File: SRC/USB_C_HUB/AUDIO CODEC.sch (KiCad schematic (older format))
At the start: 16 parts, among them IC6 ADAU1961WBCPZ-R7, J9 AudioJack2_Ground

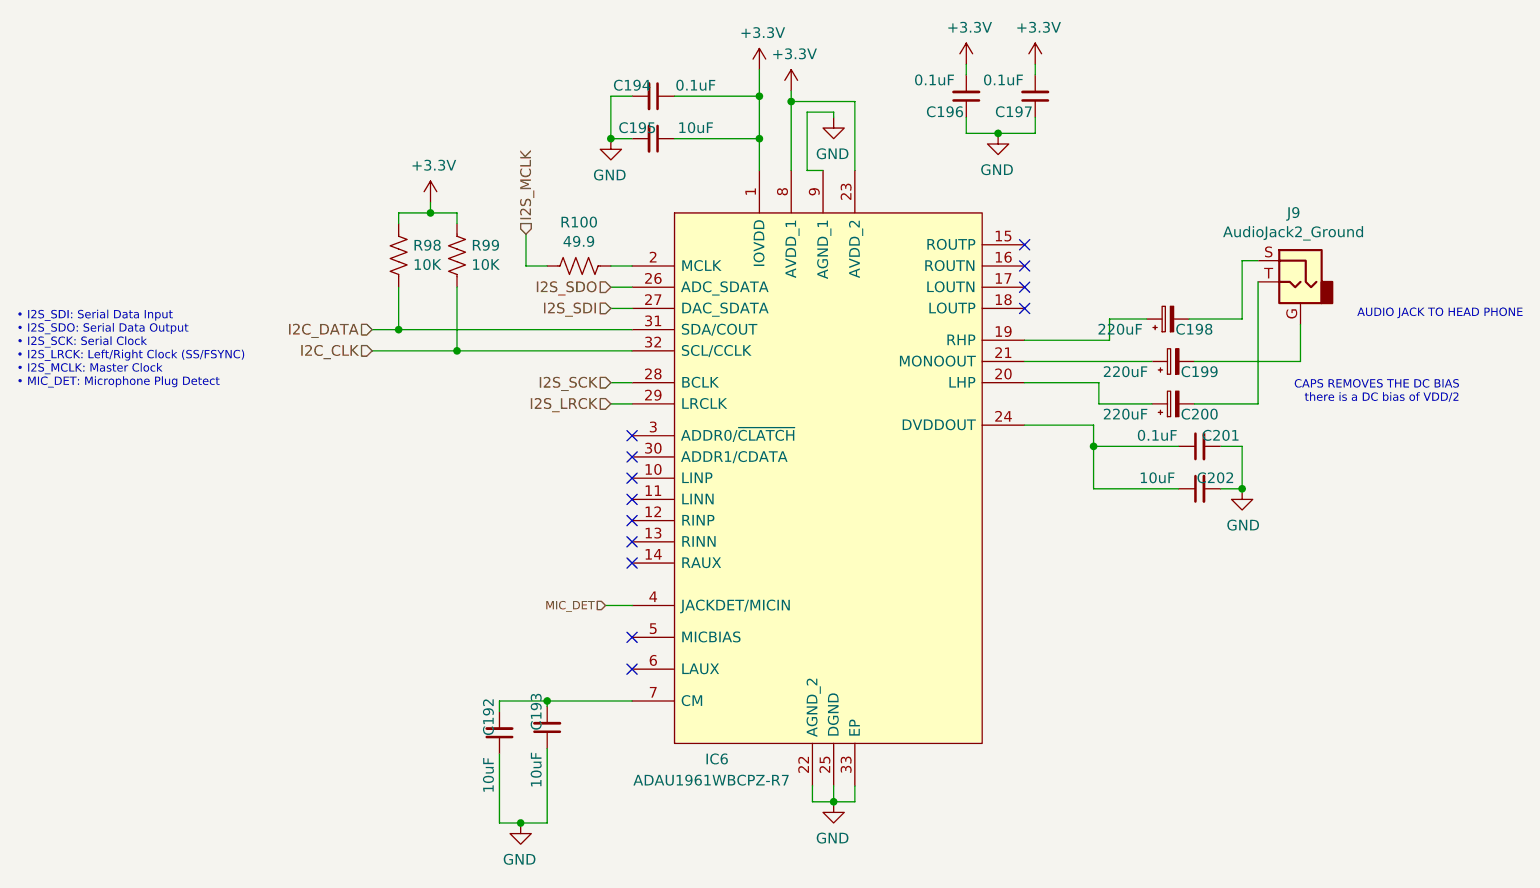
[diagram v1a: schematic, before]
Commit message: schematic capture and footprint assignment complete. Pending approval
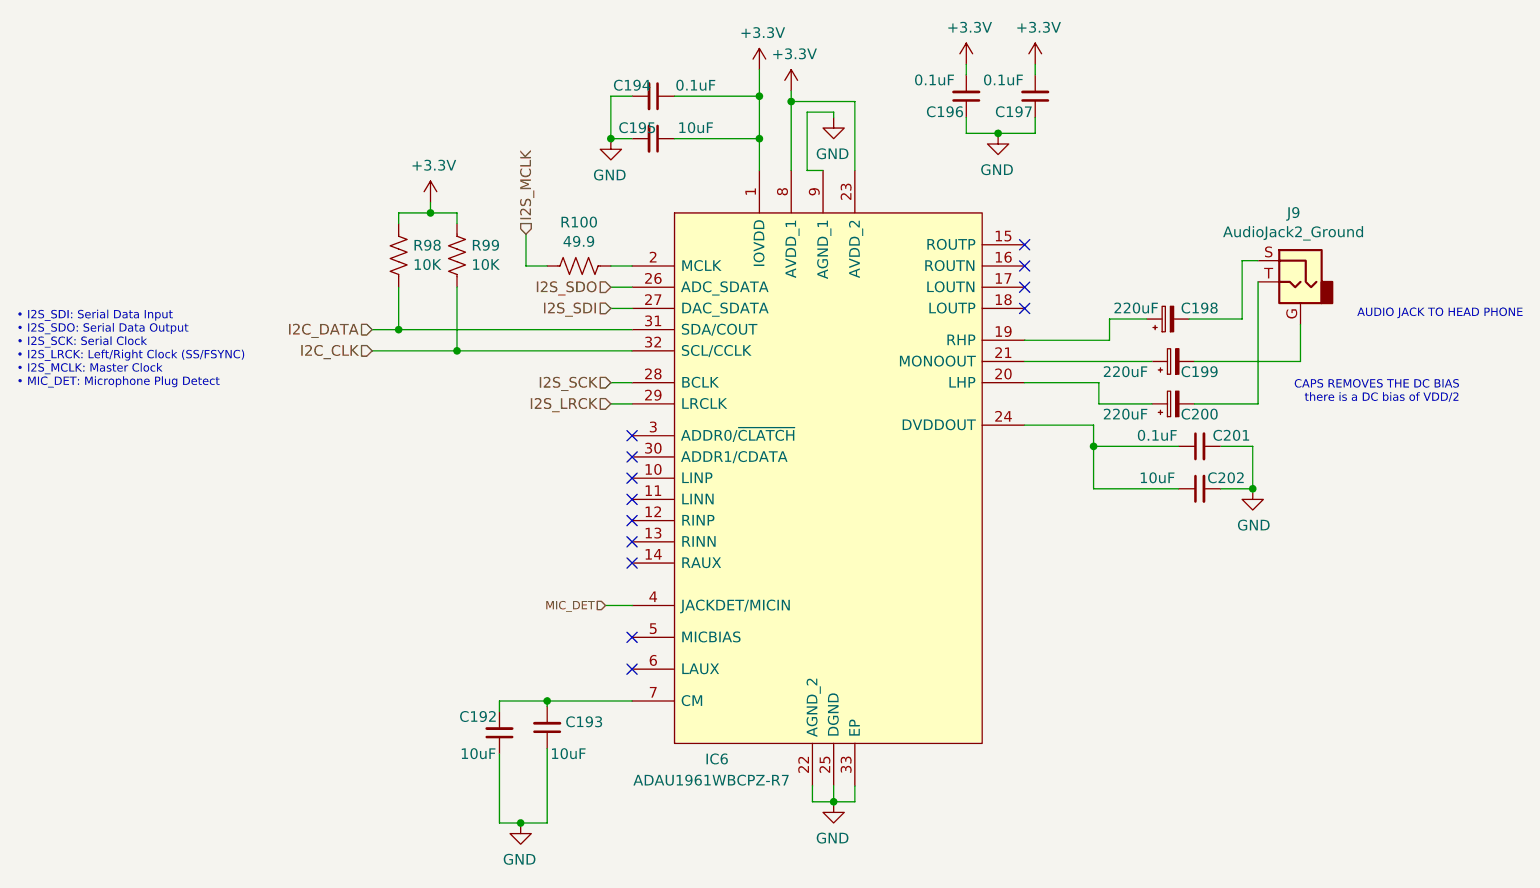
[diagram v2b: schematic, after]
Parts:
- C192, C193, C202: footprint (none) -> Capacitor_SMD:C_0603_1608Metric
- C194, C195, C196, C197, C201: footprint (none) -> Capacitor_SMD:C_0402_1005Metric
- C198, C200: footprint (none) -> Capacitor_SMD:CP_Elec_5x5.9; Mfr No. (none) -> 6SVPE220MW
- C199: footprint (none) -> Capacitor_SMD:CP_Elec_5x5.9
- IC6: footprint QFN50P500X500X100-33N-D -> SamacSys_Parts_2:QFN50P500X500X100-33N-D
- J9: footprint (none) -> footprints:CUI_SJ1-3533N
- R100, R98, R99: footprint (none) -> Resistor_SMD:R_0402_1005Metric
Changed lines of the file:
@@
 F 0 "IC6" H 5900 -350 50  0000 C CNN
 F 1 "ADAU1961WBCPZ-R7" H 5875 -450 50  0000 C CNN
-F 2 "QFN50P500X500X100-33N-D" H 7350 3025 50  0001 L CNN
+F 2 "SamacSys_Parts_2:QFN50P500X500X100-33N-D" H 7350 3025 50  0001 L CNN
 F 3 "https://componentsearchengine.com/Datasheets/1/ADAU1961WBCPZ-R7.pdf" H 7350 2925 50  0001 L CNN
 F 4 "General Purpose Audio Codec 2ADC / 2DAC Ch Automotive 32-Pin LFCSP EP T/R" H 7350 2825 50  0001 L CNN "Description"
@@
 F 0 "C194" V 5550 1575 50  0000 C CNN
 F 1 "0.1uF" V 5550 1875 50  0000 C CNN
-F 2 "" H 5600 1675 50  0001 C CNN
+F 2 "Capacitor_SMD:C_0402_1005Metric" H 5600 1675 50  0001 C CNN
 F 3 "~" H 5600 1675 50  0001 C CNN
 	1    5600 1675
@@
 F 0 "C195" V 5550 1800 50  0000 C CNN
 F 1 "10uF" V 5550 2075 50  0000 C CNN
-F 2 "" H 5600 1875 50  0001 C CNN
+F 2 "Capacitor_SMD:C_0402_1005Metric" H 5600 1875 50  0001 C CNN
 F 3 "~" H 5600 1875 50  0001 C CNN
 	1    5600 1875
@@
 F 0 "C196" H 7175 1750 50  0000 C CNN
 F 1 "0.1uF" H 7225 1600 50  0000 C CNN
-F 2 "" H 7075 1675 50  0001 C CNN
+F 2 "Capacitor_SMD:C_0402_1005Metric" H 7075 1675 50  0001 C CNN
 F 3 "~" H 7075 1675 50  0001 C CNN
 	1    7075 1675
@@
 F 0 "C197" H 7500 1750 50  0000 C CNN
 F 1 "0.1uF" H 7550 1600 50  0000 C CNN
-F 2 "" H 7400 1675 50  0001 C CNN
+F 2 "Capacitor_SMD:C_0402_1005Metric" H 7400 1675 50  0001 C CNN
 F 3 "~" H 7400 1675 50  0001 C CNN
 	1    7400 1675
@@
 F 0 "R98" H 4468 2471 50  0000 L CNN
 F 1 "10K" H 4468 2380 50  0000 L CNN
-F 2 "" V 4440 2415 50  0001 C CNN
+F 2 "Resistor_SMD:R_0402_1005Metric" V 4440 2415 50  0001 C CNN
 F 3 "~" H 4400 2425 50  0001 C CNN
 	1    4400 2425
@@
 F 0 "R99" H 4743 2471 50  0000 L CNN
 F 1 "10K" H 4743 2380 50  0000 L CNN
-F 2 "" V 4715 2415 50  0001 C CNN
+F 2 "Resistor_SMD:R_0402_1005Metric" V 4715 2415 50  0001 C CNN
 F 3 "~" H 4675 2425 50  0001 C CNN
 	1    4675 2425
@@
 F 0 "R100" V 5455 2475 50  0000 C CNN
 F 1 "49.9" V 5364 2475 50  0000 C CNN
-F 2 "" V 5290 2465 50  0001 C CNN
+F 2 "Resistor_SMD:R_0402_1005Metric" V 5290 2465 50  0001 C CNN
 F 3 "~" H 5250 2475 50  0001 C CNN
 	1    5250 2475
@@
 F 0 "J9" H 8682 2875 50  0000 C CNN
 F 1 "AudioJack2_Ground" H 8682 2784 50  0000 C CNN
-F 2 "" H 8650 2550 50  0001 C CNN
+F 2 "footprints:CUI_SJ1-3533N" H 8650 2550 50  0001 C CNN
 F 3 "~" H 8650 2550 50  0001 C CNN
 	1    8650 2550
@@
 F 0 "C199" V 8000 2800 50  0000 C CNN
 F 1 "220uF" V 8000 3150 50  0000 C CNN
-F 2 "" H 8050 2925 50  0001 C CNN
+F 2 "Capacitor_SMD:CP_Elec_5x5.9" H 8050 2925 50  0001 C CNN
 F 3 "~" H 8050 2925 50  0001 C CNN
 	1    8050 2925
@@
 F 0 "C200" V 8000 3000 50  0000 C CNN
 F 1 "220uF" V 8000 3350 50  0000 C CNN
-F 2 "" H 8050 3125 50  0001 C CNN
+F 2 "Capacitor_SMD:CP_Elec_5x5.9" H 8050 3125 50  0001 C CNN
 F 3 "~" H 8050 3125 50  0001 C CNN
+F 4 "6SVPE220MW" V 8050 3125 50  0001 C CNN "Mfr No."
 	1    8050 3125
 	0    -1   -1   0
@@
 U 1 1 63FED1F0
 P 8025 2725
-F 0 "C198" V 7975 2600 50  0000 C CNN
-F 1 "220uF" V 7975 2950 50  0000 C CNN
-F 2 "" H 8025 2725 50  0001 C CNN
+F 0 "C198" V 8075 2575 50  0000 C CNN
+F 1 "220uF" V 8075 2875 50  0000 C CNN
+F 2 "Capacitor_SMD:CP_Elec_5x5.9" H 8025 2725 50  0001 C CNN
 F 3 "~" H 8025 2725 50  0001 C CNN
+F 4 "6SVPE220MW" V 8025 2725 50  0001 C CNN "Mfr No."
 	1    8025 2725
 	0    -1   -1   0
@@
 L OLIMEX_Power:GND #PWR?
 U 1 1 63FF1DC0
-P 8375 3525
+P 8425 3525
 AR Path="/619540C6/63FF1DC0" Ref="#PWR?"  Part="1"
 AR Path="/63FF1DC0" Ref="#PWR?"  Part="1"
 AR Path="/63B95183/63FF1DC0" Ref="#PWR0194"  Part="1"
-F 0 "#PWR0194" H 8375 3275 50  0001 C CNN
-F 1 "GND" H 8380 3352 50  0000 C CNN
-F 2 "" H 8375 3525 60  0000 C CNN
-F 3 "" H 8375 3525 60  0000 C CNN
-	1    8375 3525
+F 0 "#PWR0194" H 8425 3275 50  0001 C CNN
+F 1 "GND" H 8430 3352 50  0000 C CNN
+F 2 "" H 8425 3525 60  0000 C CNN
+F 3 "" H 8425 3525 60  0000 C CNN
+	1    8425 3525
 	1    0    0    -1
 $EndComp
@@
 Wire Wire Line
 	8075 3325 7675 3325
-Wire Wire Line
-	8375 3325 8275 3325
-Wire Wire Line
-	8375 3525 8275 3525
 $Comp
 L Device:C_Small C?
@@
 AR Path="/63FF1DB2" Ref="C?"  Part="1"
 AR Path="/63B95183/63FF1DB2" Ref="C202"  Part="1"
-F 0 "C202" V 8125 3450 50  0000 C CNN
+F 0 "C202" V 8125 3400 50  0000 C CNN
 F 1 "10uF" V 8125 3725 50  0000 C CNN
-F 2 "" H 8175 3525 50  0001 C CNN
+F 2 "Capacitor_SMD:C_0603_1608Metric" H 8175 3525 50  0001 C CNN
 F 3 "~" H 8175 3525 50  0001 C CNN
 	1    8175 3525
@@
 AR Path="/63FF1D9A" Ref="C?"  Part="1"
 AR Path="/63B95183/63FF1D9A" Ref="C201"  Part="1"
-F 0 "C201" V 8125 3225 50  0000 C CNN
+F 0 "C201" V 8125 3175 50  0000 C CNN
 F 1 "0.1uF" V 8125 3525 50  0000 C CNN
-F 2 "" H 8175 3325 50  0001 C CNN
+F 2 "Capacitor_SMD:C_0402_1005Metric" H 8175 3325 50  0001 C CNN
 F 3 "~" H 8175 3325 50  0001 C CNN
 	1    8175 3325
@@
 	7675 3325 7675 3525
 Wire Wire Line
-	8375 3325 8375 3525
-Connection ~ 8375 3525
+	8425 3325 8425 3525
 $Comp
 L Device:C_Small C?
@@
 AR Path="/63FFC708" Ref="C?"  Part="1"
 AR Path="/63B95183/63FFC708" Ref="C192"  Part="1"
-F 0 "C192" V 4825 4600 50  0000 C CNN
-F 1 "10uF" V 4825 4875 50  0000 C CNN
-F 2 "" H 4875 4675 50  0001 C CNN
+F 0 "C192" H 4775 4600 50  0000 C CNN
+F 1 "10uF" H 4775 4775 50  0000 C CNN
+F 2 "Capacitor_SMD:C_0603_1608Metric" H 4875 4675 50  0001 C CNN
 F 3 "~" H 4875 4675 50  0001 C CNN
 	1    4875 4675
@@
 AR Path="/63FFDF8B" Ref="C?"  Part="1"
 AR Path="/63B95183/63FFDF8B" Ref="C193"  Part="1"
-F 0 "C193" V 5050 4575 50  0000 C CNN
-F 1 "10uF" V 5050 4850 50  0000 C CNN
-F 2 "" H 5100 4650 50  0001 C CNN
+F 0 "C193" H 5275 4625 50  0000 C CNN
+F 1 "10uF" H 5200 4775 50  0000 C CNN
+F 2 "Capacitor_SMD:C_0603_1608Metric" H 5100 4650 50  0001 C CNN
 F 3 "~" H 5100 4650 50  0001 C CNN
 	1    5100 4650
@@
 Text Notes 9400 3125 2    39   ~ 0
 CAPS REMOVES THE DC BIAS\nthere is a DC bias of VDD/2
+Wire Wire Line
+	8275 3525 8425 3525
+Connection ~ 8425 3525
+Wire Wire Line
+	8275 3325 8425 3325
 $EndSCHEMATC
